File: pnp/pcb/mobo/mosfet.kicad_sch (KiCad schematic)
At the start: 5 parts, among them J22 Mosfet, Q1 AO3400A

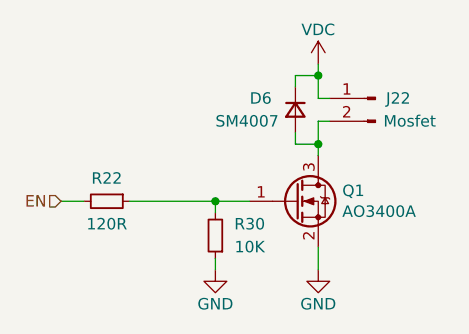
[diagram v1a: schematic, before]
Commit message: Redesign finished
Completed Board redesign and adding more EMC improvements.
Changed all the part numbers to have a Mouser orderable design (except the JST connectors)
All outputs generated
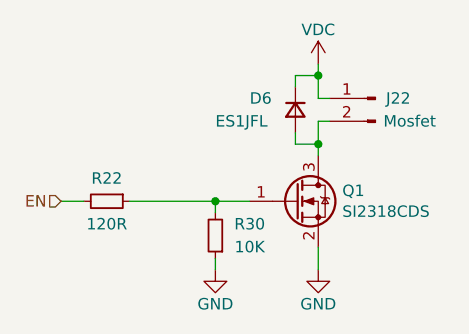
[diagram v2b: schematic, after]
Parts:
- D6: value SM4007 -> ES1JFL; Digikey SM4007PL-TPMSCT-ND -> (none); JLCPCB C64898 -> (none); LCSC C64898 -> (none); Mouser 833-SM4007PL-TP -> 512-ES1JFL
- J22: JLCPCB C20079 -> (none); LCSC C20079 -> (none); Mouser (none) -> Digikey
- Q1: value AO3400A -> SI2318CDS; Digikey IRLML6344TRPBFCT-ND -> (none); JLCPCB C332101 -> (none); LCSC C427382 -> (none); Mouser 942-IRLML6344TRPBF -> 78-SI2318CDS-T1-BE3
- R22: Digikey 541-36.0KCCT-ND -> (none); JLCPCB C4360 -> (none); LCSC C139879 -> (none); Mouser 71-CRCW080536K0FKEA -> 755-SDR10EZPF1200
- R30: Digikey 541-36.0KCCT-ND -> (none); JLCPCB C4360 -> (none); LCSC C139879 -> (none); Mouser 71-CRCW080536K0FKEA -> 603-RC0805FR-1010KL
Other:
- company: Opulo -> Opulo.io
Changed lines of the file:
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@@
   (title_block
     (title "LumenPnP Motherboard")
-    (date "2022-09-09")
-    (rev "004A")
-    (company "Opulo")
+    (date "2022-10-06")
+    (rev "04A")
+    (company "Opulo.io")
     (comment 1 "Reengineered by Magpie")
   )
@@
       (effects (font (size 1.27 1.27)) hide)
     )
-    (property "JLCPCB" "C20079" (id 4) (at 158.75 93.98 0)
-      (effects (font (size 1.27 1.27)) hide)
-    )
-    (property "LCSC" "C20079" (id 5) (at 158.75 93.98 0)
+    (property "JLCPCB" "" (id 4) (at 158.75 93.98 0)
+      (effects (font (size 1.27 1.27)) hide)
+    )
+    (property "LCSC" "" (id 5) (at 158.75 93.98 0)
       (effects (font (size 1.27 1.27)) hide)
     )
@@
       (effects (font (size 1.27 1.27)) hide)
     )
+    (property "Mouser" "Digikey" (id 7) (at 158.75 93.98 0)
+      (effects (font (size 1.27 1.27)) hide)
+    )
     (pin "1")
     (pin "2")
@@
       (effects (font (size 1.27 1.27)) (justify left))
     )
-    (property "Value" "AO3400A" (id 1) (at 155.067 106.553 0)
+    (property "Value" "SI2318CDS" (id 1) (at 155.067 106.553 0)
       (effects (font (size 1.27 1.27)) (justify left))
     )
@@
       (effects (font (size 1.27 1.27) italic) (justify left) hide)
     )
-    (property "Datasheet" "http://www.aosmd.com/pdfs/datasheet/AO3400A.pdf" (id 3) (at 149.86 105.41 0)
+    (property "Datasheet" "" (id 3) (at 149.86 105.41 0)
       (effects (font (size 1.27 1.27)) (justify left) hide)
     )
-    (property "Mouser" "942-IRLML6344TRPBF" (id 4) (at 149.86 105.41 0)
-      (effects (font (size 1.27 1.27)) hide)
-    )
-    (property "LCSC" "C427382" (id 5) (at 149.86 105.41 0)
-      (effects (font (size 1.27 1.27)) hide)
-    )
-    (property "JLCPCB" "C332101" (id 6) (at 149.86 105.41 0)
-      (effects (font (size 1.27 1.27)) hide)
-    )
-    (property "Digikey" "IRLML6344TRPBFCT-ND" (id 7) (at 149.86 105.41 0)
+    (property "Mouser" "78-SI2318CDS-T1-BE3" (id 4) (at 149.86 105.41 0)
+      (effects (font (size 1.27 1.27)) hide)
+    )
+    (property "LCSC" "" (id 5) (at 149.86 105.41 0)
+      (effects (font (size 1.27 1.27)) hide)
+    )
+    (property "JLCPCB" "" (id 6) (at 149.86 105.41 0)
+      (effects (font (size 1.27 1.27)) hide)
+    )
+    (property "Digikey" "" (id 7) (at 149.86 105.41 0)
       (effects (font (size 1.27 1.27)) hide)
     )
@@
       (effects (font (size 1.27 1.27)) hide)
     )
-    (property "Datasheet" "https://www.vishay.com/docs/20035/dcrcwe3.pdf" (id 3) (at 140.97 109.22 0)
-      (effects (font (size 1.27 1.27)) hide)
-    )
-    (property "JLCPCB" "C4360" (id 4) (at 140.97 109.22 0)
-      (effects (font (size 1.27 1.27)) hide)
-    )
-    (property "LCSC" "C139879" (id 5) (at 140.97 109.22 0)
-      (effects (font (size 1.27 1.27)) hide)
-    )
-    (property "Digikey" "541-36.0KCCT-ND" (id 6) (at 140.97 109.22 0)
-      (effects (font (size 1.27 1.27)) hide)
-    )
-    (property "Mouser" "71-CRCW080536K0FKEA" (id 7) (at 140.97 109.22 0)
+    (property "Datasheet" "" (id 3) (at 140.97 109.22 0)
+      (effects (font (size 1.27 1.27)) hide)
+    )
+    (property "JLCPCB" "" (id 4) (at 140.97 109.22 0)
+      (effects (font (size 1.27 1.27)) hide)
+    )
+    (property "LCSC" "" (id 5) (at 140.97 109.22 0)
+      (effects (font (size 1.27 1.27)) hide)
+    )
+    (property "Digikey" "" (id 6) (at 140.97 109.22 0)
+      (effects (font (size 1.27 1.27)) hide)
+    )
+    (property "Mouser" "603-RC0805FR-1010KL" (id 7) (at 140.97 109.22 0)
       (effects (font (size 1.27 1.27)) hide)
     )
@@
       (effects (font (size 1.27 1.27)) (justify left))
     )
-    (property "Value" "SM4007" (id 1) (at 140.97 96.52 90)
+    (property "Value" "ES1JFL" (id 1) (at 140.97 96.52 90)
       (effects (font (size 1.27 1.27)) (justify left))
     )
@@
       (effects (font (size 1.27 1.27)) hide)
     )
-    (property "Datasheet" "http://cdn-reichelt.de/documents/datenblatt/A400/SMD1N400%23DIO.pdf" (id 3) (at 149.86 95.25 0)
-      (effects (font (size 1.27 1.27)) hide)
-    )
-    (property "JLCPCB" "C64898" (id 4) (at 149.86 95.25 0)
-      (effects (font (size 1.27 1.27)) hide)
-    )
-    (property "LCSC" "C64898" (id 5) (at 149.86 95.25 0)
-      (effects (font (size 1.27 1.27)) hide)
-    )
-    (property "Digikey" "SM4007PL-TPMSCT-ND" (id 6) (at 149.86 95.25 0)
-      (effects (font (size 1.27 1.27)) hide)
-    )
-    (property "Mouser" "833-SM4007PL-TP" (id 7) (at 149.86 95.25 0)
+    (property "Datasheet" "" (id 3) (at 149.86 95.25 0)
+      (effects (font (size 1.27 1.27)) hide)
+    )
+    (property "JLCPCB" "" (id 4) (at 149.86 95.25 0)
+      (effects (font (size 1.27 1.27)) hide)
+    )
+    (property "LCSC" "" (id 5) (at 149.86 95.25 0)
+      (effects (font (size 1.27 1.27)) hide)
+    )
+    (property "Digikey" "" (id 6) (at 149.86 95.25 0)
+      (effects (font (size 1.27 1.27)) hide)
+    )
+    (property "Mouser" "512-ES1JFL" (id 7) (at 149.86 95.25 0)
       (effects (font (size 1.27 1.27)) hide)
     )
@@
       (effects (font (size 1.27 1.27)) hide)
     )
-    (property "Datasheet" "https://www.vishay.com/docs/20035/dcrcwe3.pdf" (id 3) (at 128.905 105.41 0)
-      (effects (font (size 1.27 1.27)) hide)
-    )
-    (property "JLCPCB" "C4360" (id 4) (at 128.905 105.41 0)
-      (effects (font (size 1.27 1.27)) hide)
-    )
-    (property "LCSC" "C139879" (id 5) (at 128.905 105.41 0)
-      (effects (font (size 1.27 1.27)) hide)
-    )
-    (property "Digikey" "541-36.0KCCT-ND" (id 6) (at 128.905 105.41 0)
-      (effects (font (size 1.27 1.27)) hide)
-    )
-    (property "Mouser" "71-CRCW080536K0FKEA" (id 7) (at 128.905 105.41 0)
-      (effects (font (size 1.27 1.27)) hide)
-    )
+    (property "Datasheet" "" (id 3) (at 128.905 105.41 0)
+      (effects (font (size 1.27 1.27)) hide)
+    )
+    (property "JLCPCB" "" (id 4) (at 128.905 105.41 0)
+      (effects (font (size 1.27 1.27)) hide)
+    )
+    (property "LCSC" "" (id 5) (at 128.905 105.41 0)
+      (effects (font (size 1.27 1.27)) hide)
+    )
+    (property "Digikey" "" (id 6) (at 128.905 105.41 0)
+      (effects (font (size 1.27 1.27)) hide)
+    )
+    (property "Mouser" "755-SDR10EZPF1200" (id 7) (at 128.905 105.41 0)
+      (effects (font (size 1.27 1.27)) hide)
+    )
